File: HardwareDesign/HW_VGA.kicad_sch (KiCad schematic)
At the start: 4 parts, among them J401 Conn_01x06, U1 25.175 MHz, U301 GAL22V10

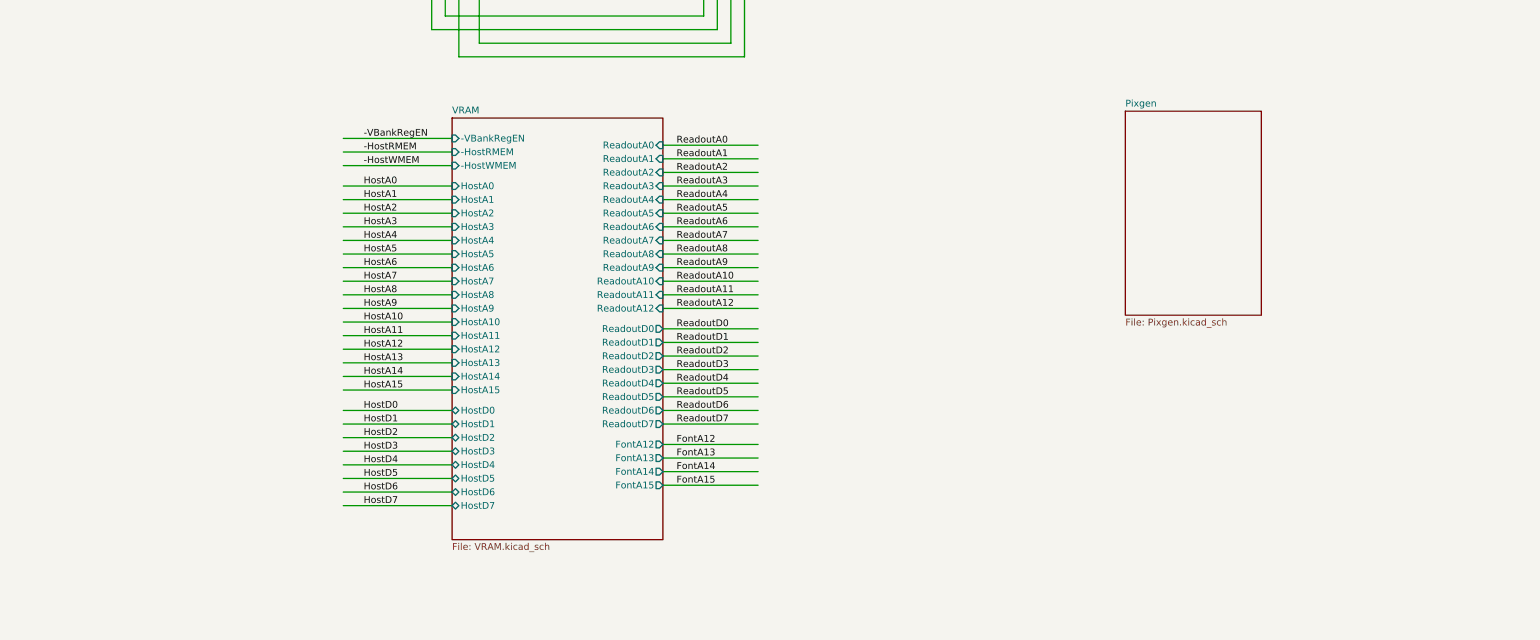
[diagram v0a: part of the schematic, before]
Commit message: starting new Readout module
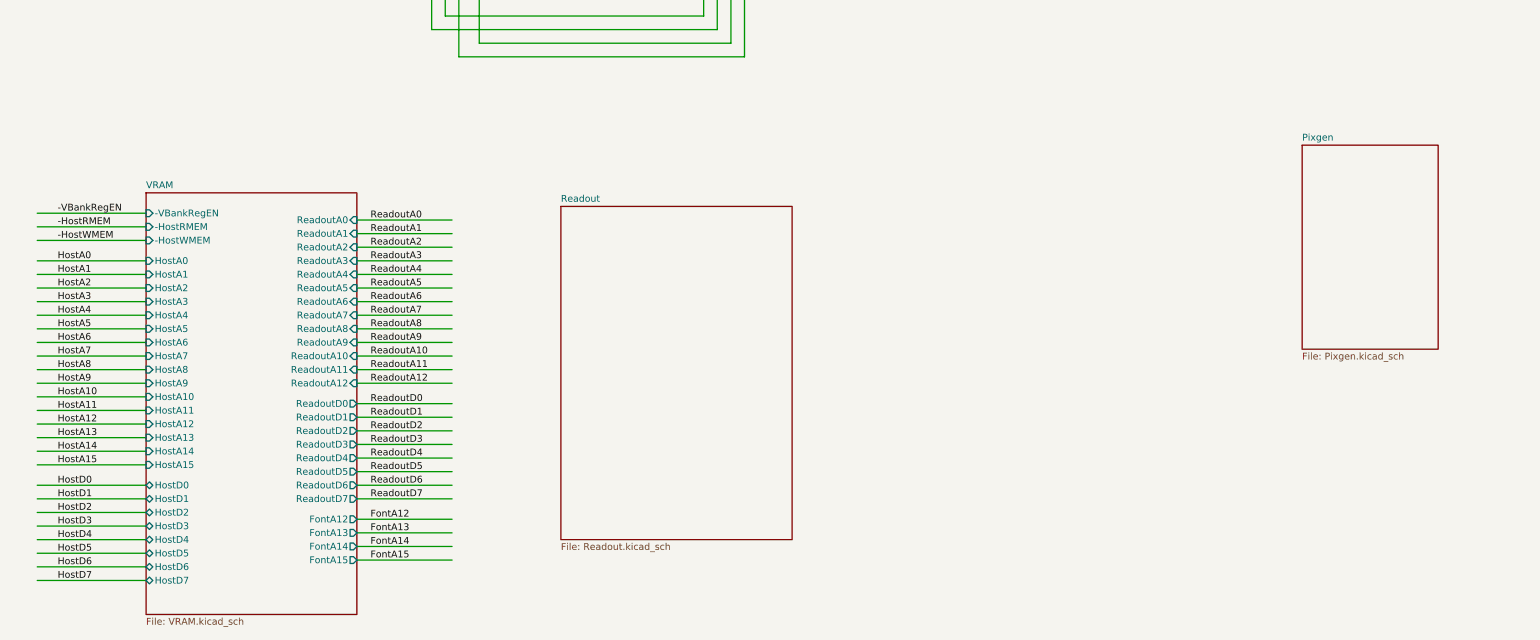
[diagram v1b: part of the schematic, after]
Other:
- added sheet Readout (Readout.kicad_sch)

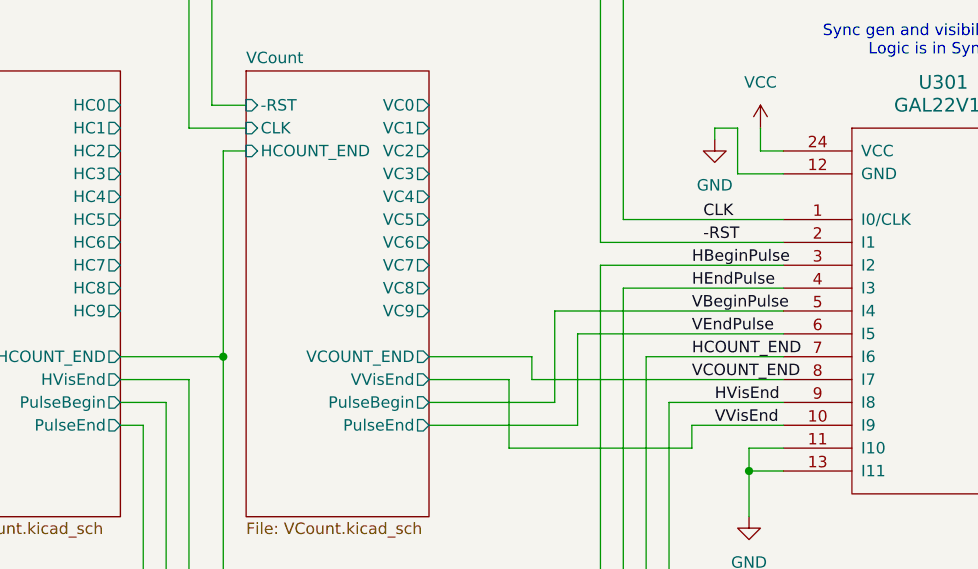
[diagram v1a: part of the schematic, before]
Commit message: revise for accurat VCOUNT mods
Will need to double check these changes.
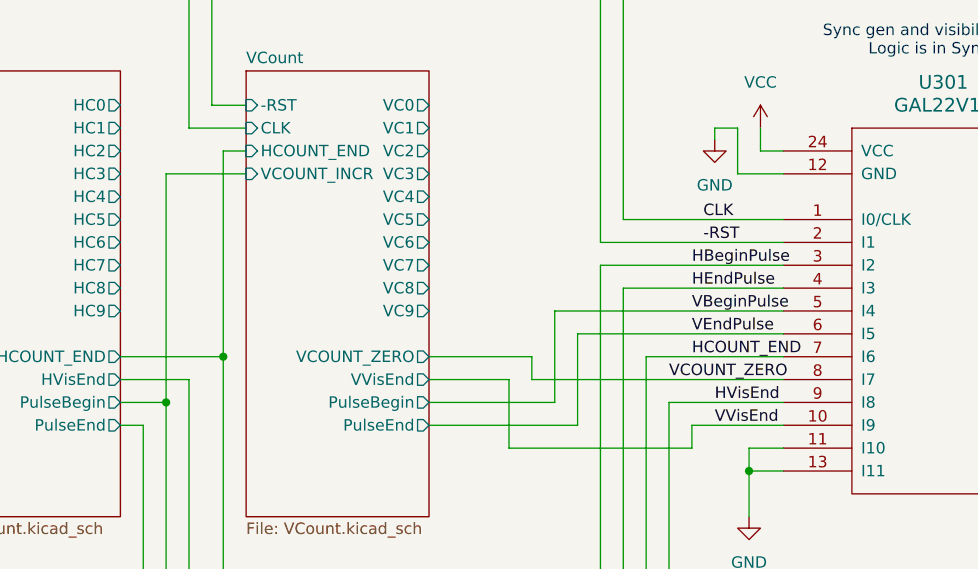
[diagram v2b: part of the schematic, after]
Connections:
- net VCOUNT_END renamed VCOUNT_ZERO
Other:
- sheet VCount ports: added VCOUNT_INCR, VCOUNT_ZERO; removed VCOUNT_END
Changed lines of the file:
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@@
 	)
 	(junction
+		(at 100.33 76.2)
+		(diameter 0)
+		(color 0 0 0 0)
+	)
+	(junction
 		(at 165.1 83.82)
 		(diameter 0)
@@
 	(wire
 		(pts
+			(xy 109.22 50.8) (xy 100.33 50.8)
+		)
+		(stroke
+			(width 0)
+			(type default)
+		)
+	)
+	(wire
+		(pts
 			(xy 97.79 104.14) (xy 151.13 104.14)
 		)
@@
 	(wire
 		(pts
+			(xy 100.33 50.8) (xy 100.33 76.2)
+		)
+		(stroke
+			(width 0)
+			(type default)
+		)
+	)
+	(wire
+		(pts
 			(xy 285.75 52.07) (xy 302.26 52.07)
 		)
@@
 		)
 	)
-	(label "VCOUNT_END"
-		(at 158.75 73.66 0)
-		(fields_autoplaced yes)
-		(effects
-			(font
-				(size 1.27 1.27)
-			)
-			(justify left bottom)
-		)
-	)
 	(label "HostA5"
 		(at 27.94 160.02 0)
@@
 		)
 	)
+	(label "VCOUNT_ZERO"
+		(at 156.21 73.66 0)
+		(fields_autoplaced yes)
+		(effects
+			(font
+				(size 1.27 1.27)
+			)
+			(justify left bottom)
+		)
+	)
 	(label "HostD4"
 		(at 27.94 199.39 0)
@@
 			)
 		)
-		(pin "VCOUNT_END" output
-			(at 129.54 71.12 0)
-			(effects
-				(font
-					(size 1.27 1.27)
-				)
-				(justify right)
-			)
-		)
 		(pin "VC4" output
 			(at 129.54 53.34 0)
@@
 			(effects
 				(font
+					(size 1.27 1.27)
+				)
+				(justify left)
+			)
+		)
+		(pin "VCOUNT_ZERO" output
+			(at 129.54 71.12 0)
+			(effects
+				(font
+					(size 1.27 1.27)
+				)
+				(justify right)
+			)
+		)
+		(pin "VCOUNT_INCR" input
+			(at 109.22 50.8 180)
+			(effects
+				(font

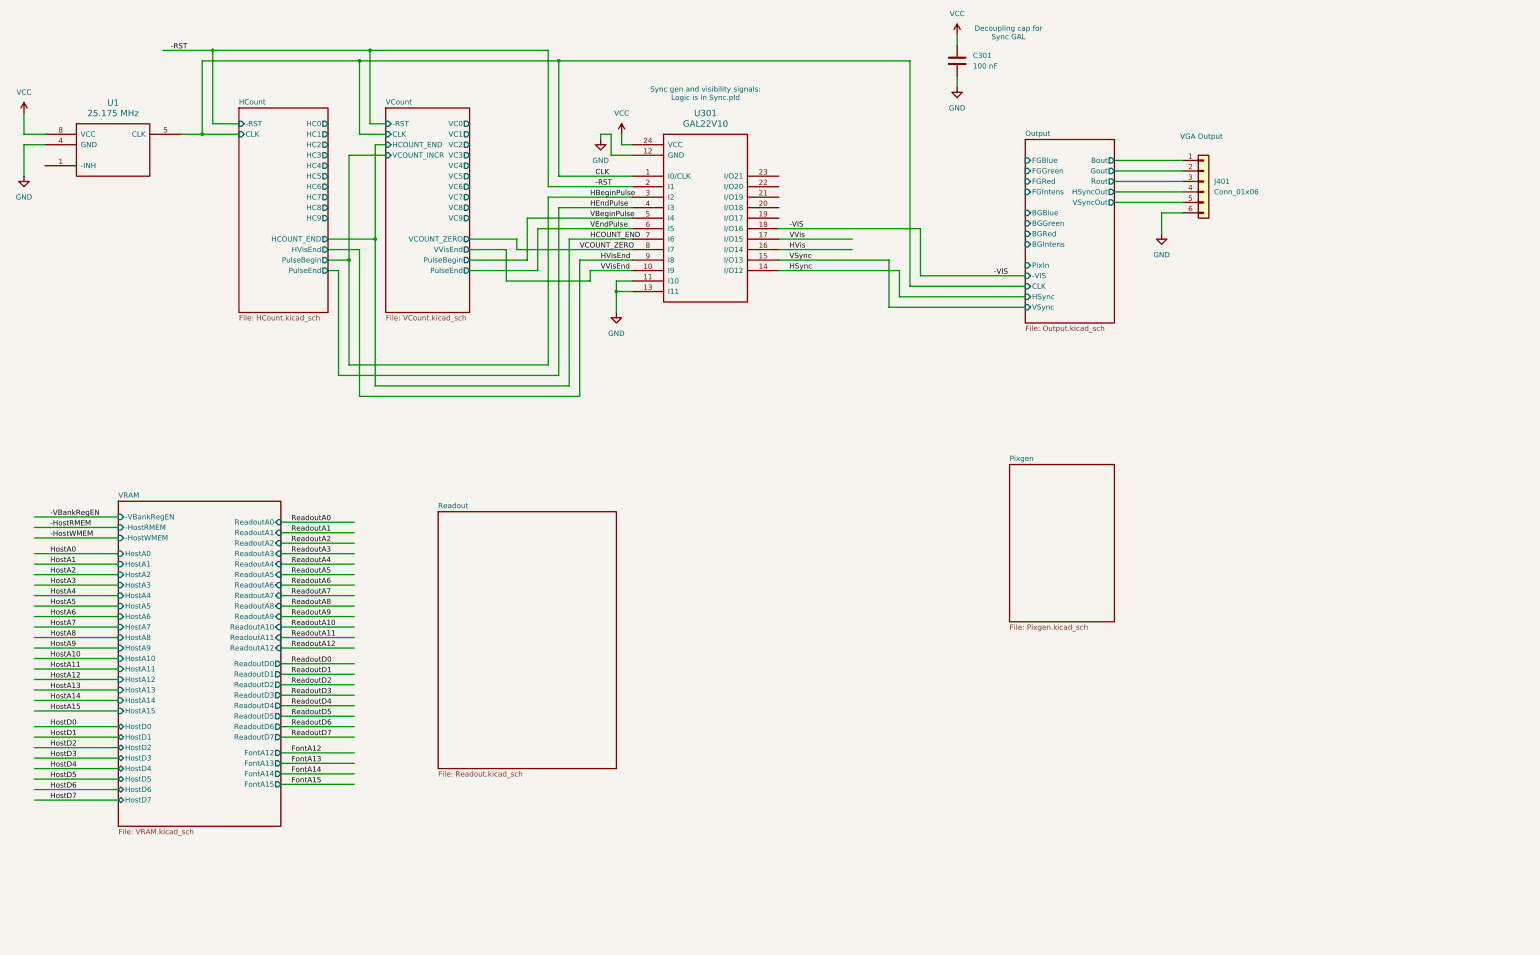
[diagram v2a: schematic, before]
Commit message: add backplane connector to main sheet
Also tidied up a few details related to hardware
changes needed for accurate VCOUNT during horizontal
visibility.
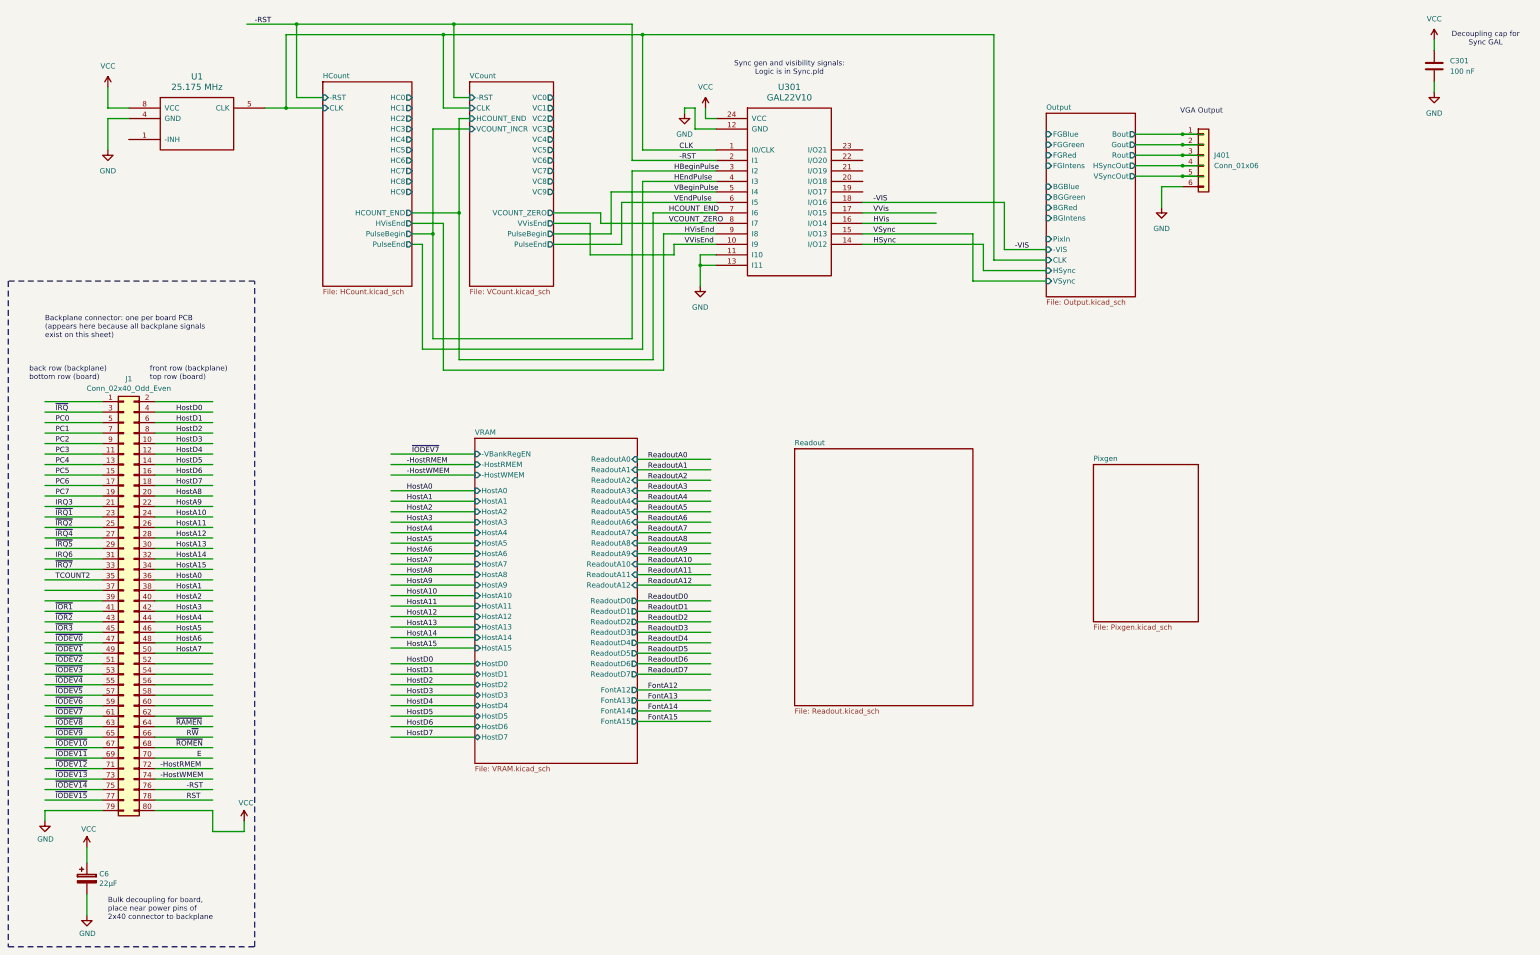
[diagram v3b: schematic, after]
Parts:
- added C6: 22μF, Capacitor_THT:CP_Radial_D6.3mm_P2.50mm, symbol device:CP
- added J1: Conn_02x40_Odd_Even, Connector_PinHeader_2.54mm:PinHeader_2x40_P2.54mm_Vertical, symbol Connector_Generic:Conn_02x40_Odd_Even
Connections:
- net -HostRMEM: now also J1.72 (Pin_72)
- net -HostWMEM: now also J1.74 (Pin_74)
- net -RST: now also J1.76 (Pin_76)
- net GND: now also C6.2, J1.79 (Pin_79)
- net HostA0: now also J1.36 (Pin_36)
- net HostA1: now also J1.38 (Pin_38)
- net HostA10: now also J1.24 (Pin_24)
- net HostA11: now also J1.26 (Pin_26)
- net HostA12: now also J1.28 (Pin_28)
- net HostA13: now also J1.30 (Pin_30)
- net HostA14: now also J1.32 (Pin_32)
- net HostA15: now also J1.34 (Pin_34)
- net HostA2: now also J1.40 (Pin_40)
- net HostA3: now also J1.42 (Pin_42)
- net HostA4: now also J1.44 (Pin_44)
- net HostA5: now also J1.46 (Pin_46)
- net HostA6: now also J1.48 (Pin_48)
- net HostA7: now also J1.50 (Pin_50)
- net HostA8: now also J1.20 (Pin_20)
- net HostA9: now also J1.22 (Pin_22)
- net HostD0: now also J1.4 (Pin_4)
- net HostD1: now also J1.6 (Pin_6)
- net HostD2: now also J1.8 (Pin_8)
- net HostD3: now also J1.10 (Pin_10)
- net HostD4: now also J1.12 (Pin_12)
- net HostD5: now also J1.14 (Pin_14)
- net HostD6: now also J1.16 (Pin_16)
- net HostD7: now also J1.18 (Pin_18)
- net VCC: now also C6.1, J1.80 (Pin_80)
- new net E: J1.70 (Pin_70)
- new net IRQ3: J1.21 (Pin_21)
- new net IRQ6: J1.31 (Pin_31)
- new net PC0: J1.5 (Pin_5)
- new net PC1: J1.7 (Pin_7)
- new net PC2: J1.9 (Pin_9)
- new net PC3: J1.11 (Pin_11)
- new net PC4: J1.13 (Pin_13)
- new net PC5: J1.15 (Pin_15)
- new net PC6: J1.17 (Pin_17)
- new net PC7: J1.19 (Pin_19)
- new net RST: J1.78 (Pin_78)
- new net R~{W}: J1.66 (Pin_66)
- new net TCOUNT2: J1.35 (Pin_35)
- new net ~{IODEV0}: J1.47 (Pin_47)
- new net ~{IODEV10}: J1.67 (Pin_67)
- new net ~{IODEV11}: J1.69 (Pin_69)
- new net ~{IODEV12}: J1.71 (Pin_71)
- new net ~{IODEV13}: J1.73 (Pin_73)
- new net ~{IODEV14}: J1.75 (Pin_75)
- new net ~{IODEV15}: J1.77 (Pin_77)
- new net ~{IODEV1}: J1.49 (Pin_49)
- new net ~{IODEV2}: J1.51 (Pin_51)
- new net ~{IODEV3}: J1.53 (Pin_53)
- new net ~{IODEV4}: J1.55 (Pin_55)
- new net ~{IODEV5}: J1.57 (Pin_57)
- new net ~{IODEV6}: J1.59 (Pin_59)
- new net ~{IODEV7}: J1.61 (Pin_61)
- new net ~{IODEV8}: J1.63 (Pin_63)
- new net ~{IODEV9}: J1.65 (Pin_65)
- new net ~{IOR1}: J1.41 (Pin_41)
- new net ~{IOR2}: J1.43 (Pin_43)
- new net ~{IOR3}: J1.45 (Pin_45)
- new net ~{IRQ1}: J1.23 (Pin_23)
- new net ~{IRQ2}: J1.25 (Pin_25)
- new net ~{IRQ4}: J1.27 (Pin_27)
- new net ~{IRQ5}: J1.29 (Pin_29)
- new net ~{IRQ7}: J1.33 (Pin_33)
- new net ~{IRQ}: J1.3 (Pin_3)
- new net ~{RAMEN}: J1.64 (Pin_64)
- new net ~{ROMEN}: J1.68 (Pin_68)
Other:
- note added: "Backplane connector: one per board PCB (appears here because all backplane signals exist on this sheet)"
- note added: "Bulk decoupling for board, place near power pins of 2x40 connector to backplane"
- note added: "back row (backplane) bottom row (board)"
- note added: "front row (backplane) top row (board)"
- moved on the sheet: C301, J401, U1, U301

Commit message: more updates to add changes from sim
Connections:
- net GND: no longer U301.11 (I10), U301.13 (I11)
- new net VCount/VCOUNT_END: U301.11 (I10)
- new net VCount/VEndActive: U301.13 (I11)
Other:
- sheet Readout ports: added -RST, CLK, HBeginActive, HBeginPulse, HEndActive, ReadoutA0, ReadoutA1, ReadoutA10, ReadoutA11, ReadoutA12, ReadoutA2, ReadoutA3, ReadoutA4, ReadoutA5, ReadoutA6, ReadoutA7, ReadoutA8, ReadoutA9, RowBeginA12, VActive, VC0, VC1, VC2, VC3, VSync; removed none
- sheet VCount ports: added VCOUNT_END, VEndActive; removed none
